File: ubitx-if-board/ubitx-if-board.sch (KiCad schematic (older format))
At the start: 42 parts, among them J1 Signal, J2 Power, J3 RX IN, J4 RX OUT, J5 TX IN, J6 TX OUT, Q101 BFR92, Q102 BFR92, Q103 BFR92, Q201 BFR92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

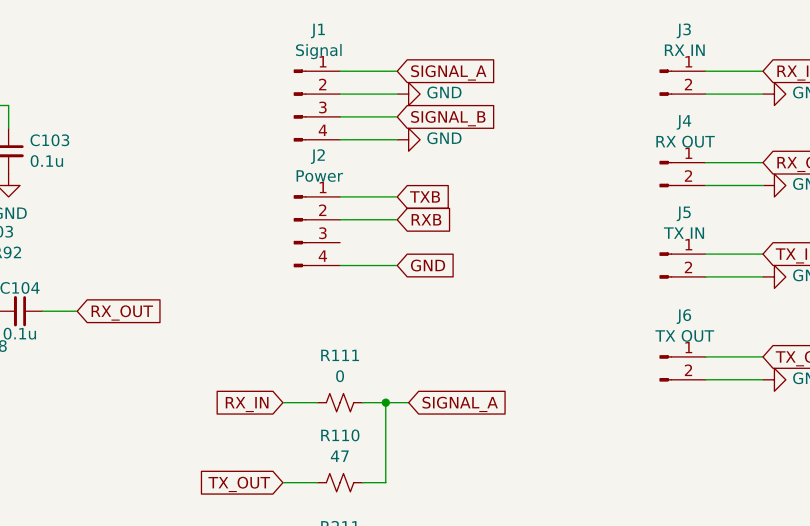
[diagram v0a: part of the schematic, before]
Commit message: * whoops, use a proper ground * make txb/rxb a pair of pairs, in case they want to be wired/powered   via two separate connections (ie, as independent IF amplifiers)   rather than expecting TXB/RXB to be routed together in cables.
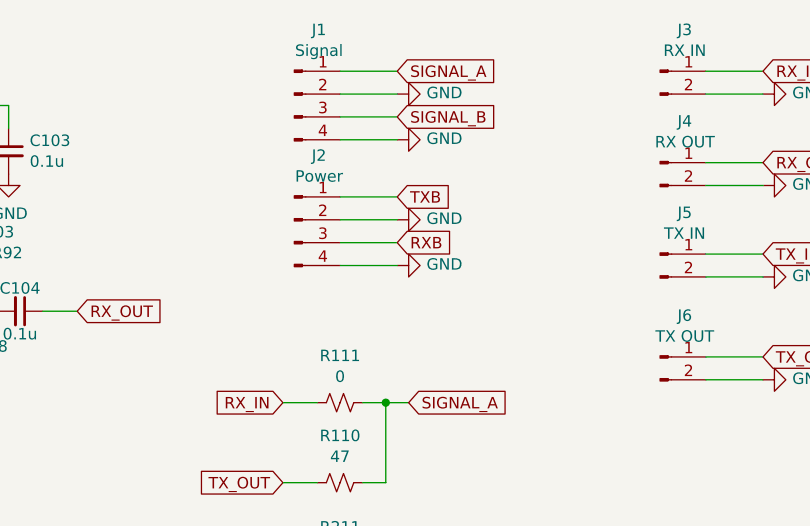
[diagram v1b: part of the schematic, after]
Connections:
- net GND: now also J2.2 (Pin_2)
- net RXB: now also J2.3 (Pin_3); no longer J2.2 (Pin_2)
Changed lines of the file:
@@
 Text GLabel 6100 1500 2    50   Input ~ 0
 TXB
-Text GLabel 6100 1600 2    50   Input ~ 0
+Text GLabel 6100 1700 2    50   Input ~ 0
 RXB
-Text GLabel 6100 1800 2    50   Input ~ 0
-GND
 $Comp
 L Connector:Conn_01x04_Male J1
@@
 Wire Wire Line
 	6100 1600 5850 1600
-Wire Wire Line
-	6100 1800 5850 1800
 Text GLabel 5600 2400 0    50   Input ~ 0
 RX_IN
@@
 	0    -1   -1   0
 $EndComp
+Wire Wire Line
+	6100 1700 5850 1700
+$Comp
+L power:GND #PWR?
+U 1 1 6063BAAB
+P 6100 1600
+F 0 "#PWR?" H 6100 1350 50  0001 C CNN
+F 1 "GND" V 6105 1472 50  0000 R CNN
+F 2 "" H 6100 1600 50  0001 C CNN
+F 3 "" H 6100 1600 50  0001 C CNN
+	1    6100 1600
+	0    -1   -1   0
+$EndComp
+$Comp
+L power:GND #PWR?
+U 1 1 6063E5FC
+P 6100 1800
+F 0 "#PWR?" H 6100 1550 50  0001 C CNN
+F 1 "GND" V 6105 1672 50  0000 R CNN
+F 2 "" H 6100 1800 50  0001 C CNN
+F 3 "" H 6100 1800 50  0001 C CNN
+	1    6100 1800
+	0    -1   -1   0
+$EndComp
+Wire Wire Line
+	5850 1800 6100 1800
 $EndSCHEMATC

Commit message: * add net file * update an actual routed pcb, need to fix labels and put my name on it
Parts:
- C101, C102, C103, C104, C201, C202, C203, C204: footprint (none) -> Capacitor_SMD:C_0603_1608Metric_Pad1.08x0.95mm_HandSolder
- J1, J2: footprint (none) -> Connector_PinHeader_2.54mm:PinHeader_1x04_P2.54mm_Vertical
- J3, J4, J5, J6: footprint (none) -> Connector_PinHeader_2.54mm:PinHeader_1x02_P2.54mm_Vertical
- L101, L201: footprint (none) -> Inductor_SMD:L_1210_3225Metric_Pad1.42x2.65mm_HandSolder
- R101, R102, R103, R104, R105, R106, R107, R108, R110, R111, R201, R202, R203, R204, R205, R206, R207, R208, R210, R211: footprint (none) -> Resistor_SMD:R_0603_1608Metric_Pad0.98x0.95mm_HandSolder

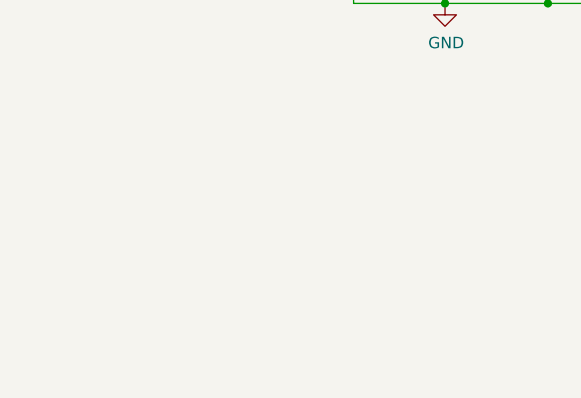
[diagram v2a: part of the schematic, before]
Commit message: WHOOPS - my last minute vias were err, wrong.
THIS is now what's sent as v1.0 to print at oshpark!
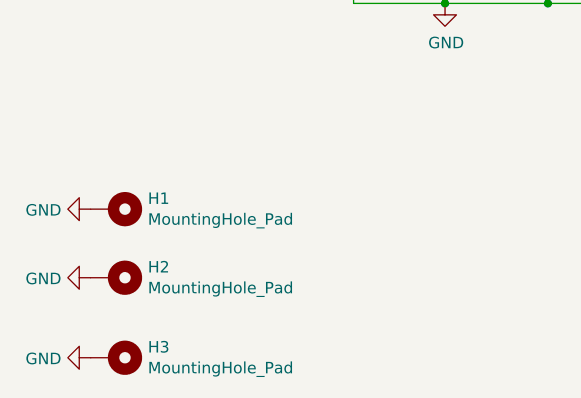
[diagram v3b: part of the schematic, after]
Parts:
- added H1, H2, H3: MountingHole_Pad, MountingHole:MountingHole_2.2mm_M2_DIN965_Pad_TopBottom, symbol Mechanical:MountingHole_Pad
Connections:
- net GND: now also H1.1, H2.1, H3.1
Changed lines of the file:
@@
 	1    0    0    -1
 $EndComp
+$Comp
+L Mechanical:MountingHole_Pad H1
+U 1 1 60528168
+P 1550 5400
+F 0 "H1" V 1504 5550 50  0000 L CNN
+F 1 "MountingHole_Pad" V 1595 5550 50  0000 L CNN
+F 2 "MountingHole:MountingHole_2.2mm_M2_DIN965_Pad_TopBottom" H 1550 5400 50  0001 C CNN
+F 3 "~" H 1550 5400 50  0001 C CNN
+	1    1550 5400
+	0    1    1    0
+$EndComp
+$Comp
+L Mechanical:MountingHole_Pad H2
+U 1 1 6052991B
+P 1550 5700
+F 0 "H2" V 1504 5850 50  0000 L CNN
+F 1 "MountingHole_Pad" V 1595 5850 50  0000 L CNN
+F 2 "MountingHole:MountingHole_2.2mm_M2_DIN965_Pad_TopBottom" H 1550 5700 50  0001 C CNN
+F 3 "~" H 1550 5700 50  0001 C CNN
+	1    1550 5700
+	0    1    1    0
+$EndComp
+$Comp
+L Mechanical:MountingHole_Pad H3
+U 1 1 6052CA65
+P 1550 6050
+F 0 "H3" V 1504 6200 50  0000 L CNN
+F 1 "MountingHole_Pad" V 1595 6200 50  0000 L CNN
+F 2 "MountingHole:MountingHole_2.2mm_M2_DIN965_Pad_TopBottom" H 1550 6050 50  0001 C CNN
+F 3 "~" H 1550 6050 50  0001 C CNN
+	1    1550 6050
+	0    1    1    0
+$EndComp
+$Comp
+L power:GND #PWR0113
+U 1 1 60537FEC
+P 1450 5400
+F 0 "#PWR0113" H 1450 5150 50  0001 C CNN
+F 1 "GND" V 1455 5272 50  0000 R CNN
+F 2 "" H 1450 5400 50  0001 C CNN
+F 3 "" H 1450 5400 50  0001 C CNN
+	1    1450 5400
+	0    1    1    0
+$EndComp
+$Comp
+L power:GND #PWR0114
+U 1 1 60538857
+P 1450 5700
+F 0 "#PWR0114" H 1450 5450 50  0001 C CNN
+F 1 "GND" V 1455 5572 50  0000 R CNN
+F 2 "" H 1450 5700 50  0001 C CNN
+F 3 "" H 1450 5700 50  0001 C CNN
+	1    1450 5700
+	0    1    1    0
+$EndComp
+$Comp
+L power:GND #PWR0115
+U 1 1 6053B45F
+P 1450 6050
+F 0 "#PWR0115" H 1450 5800 50  0001 C CNN
+F 1 "GND" V 1455 5922 50  0000 R CNN
+F 2 "" H 1450 6050 50  0001 C CNN
+F 3 "" H 1450 6050 50  0001 C CNN
+	1    1450 6050
+	0    1    1    0
+$EndComp
 $EndSCHEMATC
